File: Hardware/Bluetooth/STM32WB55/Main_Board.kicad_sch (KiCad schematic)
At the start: 11 parts, among them J9 Conn_01x02_Pin, SW1 SW_Wurth, U2 INA240A1PW

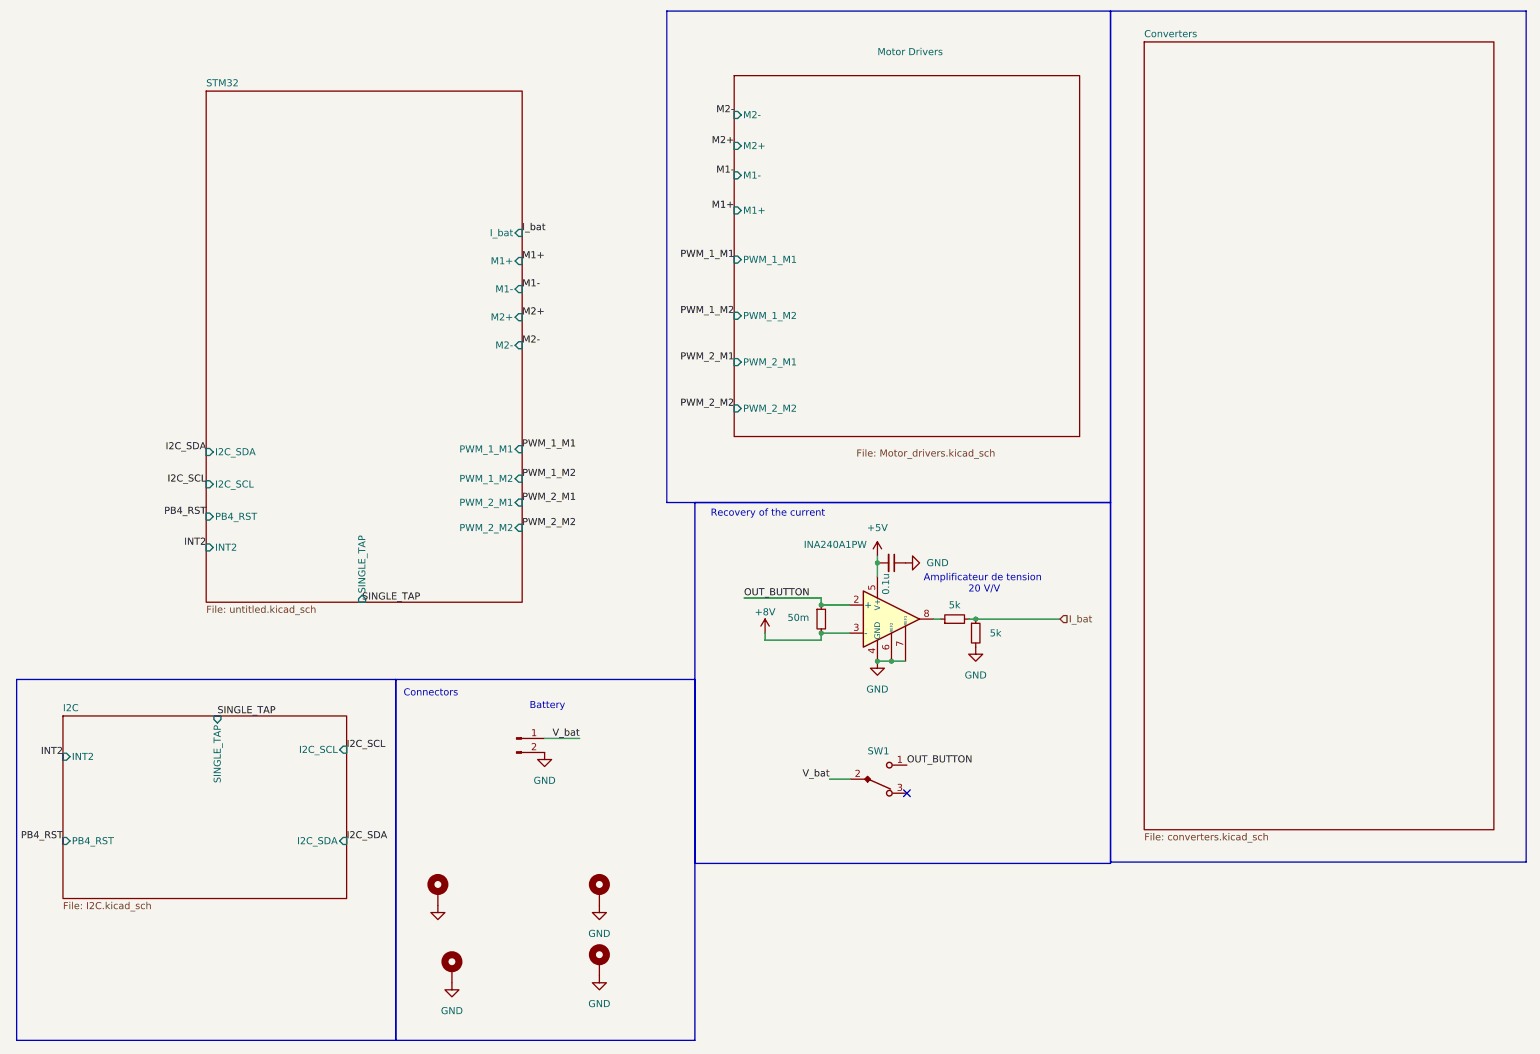
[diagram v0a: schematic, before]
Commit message: schematic update
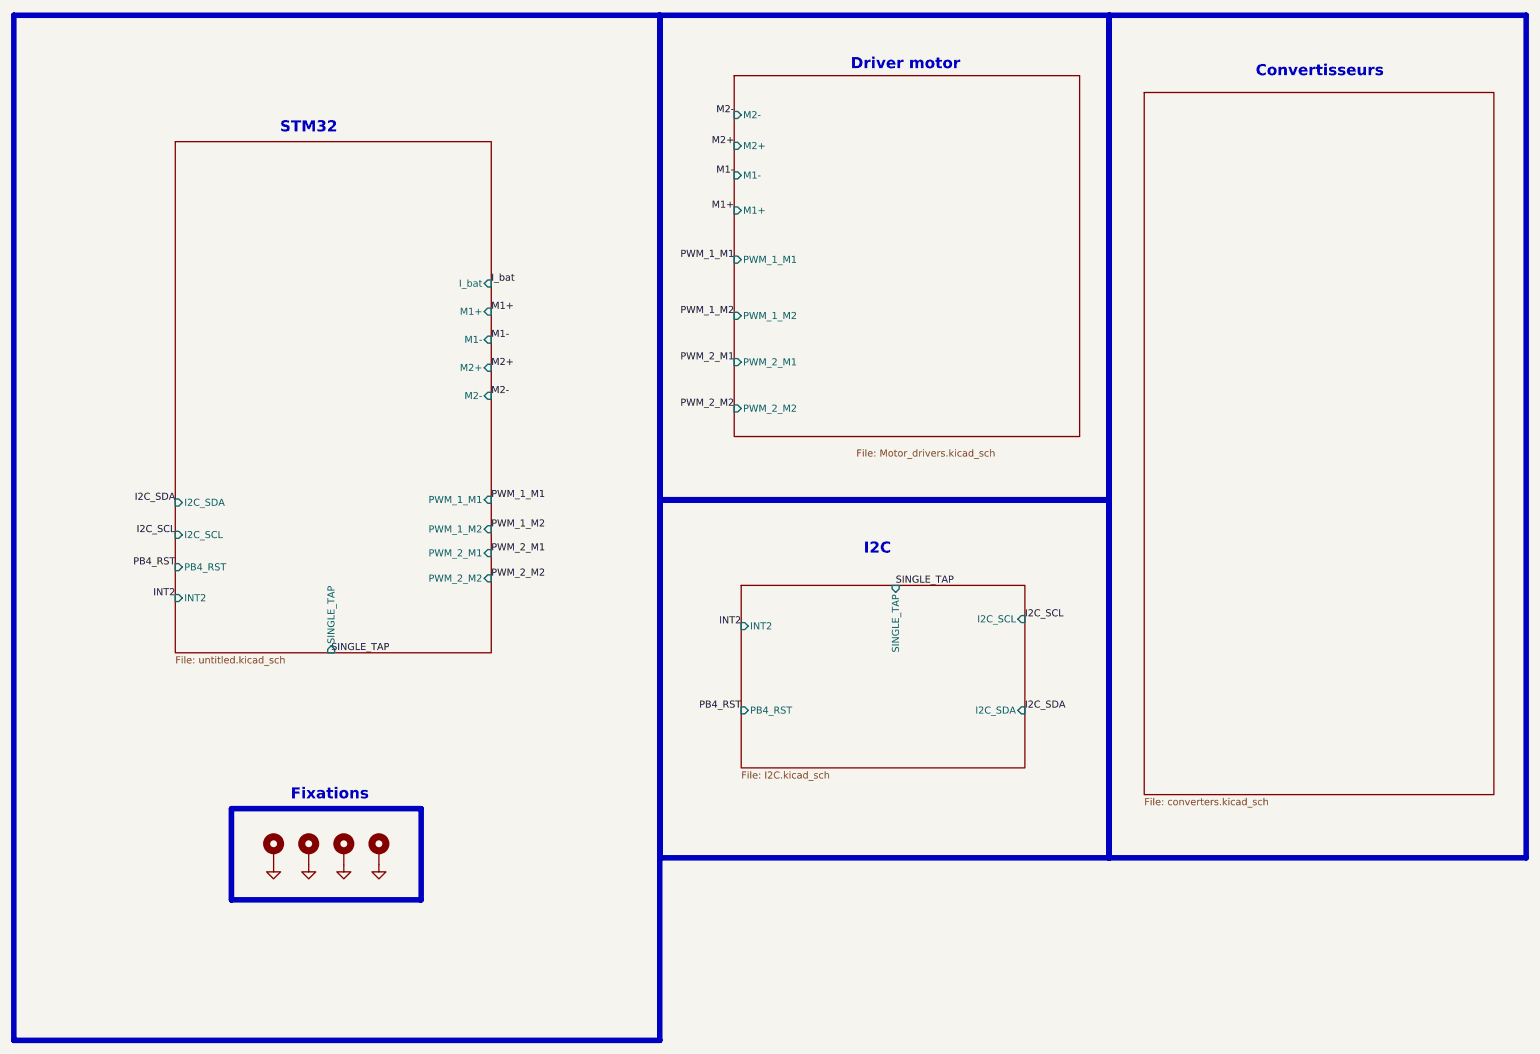
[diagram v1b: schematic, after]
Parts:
- removed C35: 0.1u, Capacitor_SMD:C_0603_1608Metric, symbol Device:C_Small
- removed J9: Conn_01x02_Pin, Connector_JST:JST_XH_B2B-XH-A_1x02_P2.50mm_Vertical, symbol Connector:Conn_01x02_Pin
- removed R15: 50m, Resistor_SMD:R_6431, symbol Device:R_Small
- removed R16, R17: 5k, Resistor_SMD:R_0603_1608Metric, symbol Device:R_Small
- removed SW1: SW_Wurth, Button_Switch_THT:SW_Wurth_WS-TOTV_472121020311, symbol Switch:SW_Wurth
- removed U2: INA240A1PW, Package_SO:TSSOP-8_4.4x3mm_P0.65mm, symbol Amplifier_Current:INA240A1PW
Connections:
- no-connect marks 1 -> 0
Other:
- note added: "Convertisseurs"
- note added: "Driver motor"
- note added: "Fixations"
- note added: "I2C"
- note added: "STM32"
- note removed: "Amplificateur de tension 20 V/V"
- note removed: "Battery"
- note removed: "Connectors"
- note removed: "Recovery of the current"

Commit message: clean
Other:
- sheet Converters ports: added I_bat; removed none
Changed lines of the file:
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@@
+	)
+	(label "I_bat"
+		(at 220.98 124.46 180)
+		(effects
+			(font
+				(size 1.27 1.27)
+			)
+			(justify right bottom)
+		)
 	)
 	(label "I_bat"
@@
 	)
 	(sheet
-		(at 215.9 26.67)
-		(size 63.246 127)
+		(at 220.98 26.67)
+		(size 58.166 127)
 		(exclude_from_sim no)
 		(in_bom yes)
@@
 		)
 		(property "Sheetname" "Converters"
-			(at 215.9 25.9584 0)
+			(at 220.98 25.9584 0)
 			(effects
 				(font
@@
 		)
 		(property "Sheetfile" "converters.kicad_sch"
-			(at 215.9 154.2546 0)
+			(at 220.98 154.2546 0)
 			(effects
 				(font
@@
 			)
 		)
+		(pin "I_bat" input
+			(at 220.98 124.46 180)
+			(effects
+				(font
+					(size 1.27 1.27)
+				)
+				(justify left)
+			)
+		)
